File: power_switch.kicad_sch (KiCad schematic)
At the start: 0 parts

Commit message: split into multiple sheets
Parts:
- added J3: Power Input, TerminalBlock_RND:TerminalBlock_RND_205-00287_1x02_P5.08mm_Horizontal, symbol Connector:Screw_Terminal_01x02
- added J4: Power Output, TerminalBlock_RND:TerminalBlock_RND_205-00287_1x02_P5.08mm_Horizontal, symbol Connector:Screw_Terminal_01x02
- added R1, R2, R3: 4.7kΩ, symbol Device:R_Small
- added R4: 1.2kΩ, symbol Device:R_Small
- added U1: BTS7004-1EPP, Package_SO:Infineon_PG-TSDSO-14-22, symbol Power_Management:BTS7004-1EPP
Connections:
- new net: R1.2, U1.2 (IN)
- new net: R3.2, R4.2, U1.4 (IS)
- new net: J4.1 (Pin_1), U1.10 (OUT), U1.12 (OUT), U1.13 (OUT), U1.14 (OUT), U1.8 (OUT), U1.9 (OUT)
- new net: R2.2, U1.3 (DEN)
- new net GND: J3.2 (Pin_2), J4.2 (Pin_2), R4.1, U1.1 (GND)
- new net SW1_ADC: R3.1
- new net SW1_DEN: R2.1
- new net SW1_IN: R1.1
- new net VDD: J3.1 (Pin_1), U1.15 (VS)
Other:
- note added: "Power Input"
- note added: "Power Switch 1"

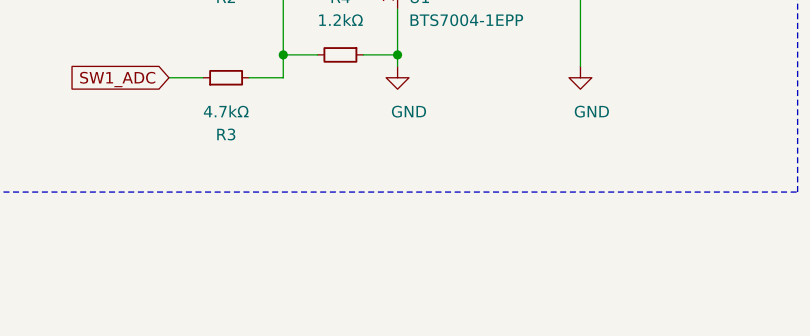
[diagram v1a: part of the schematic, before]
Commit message: use USB-C and add analog filtering
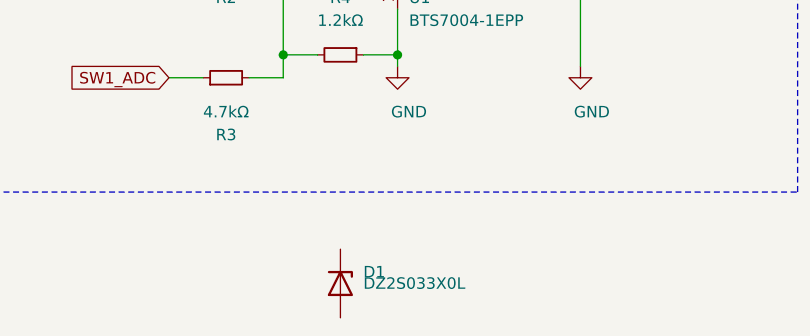
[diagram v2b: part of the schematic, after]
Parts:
- added D1: DZ2S033X0L, Diode_SMD:D_SOT-23_ANK, symbol Diode:DZ2S033X0L
- R1, R2, R3, R4: footprint (none) -> Resistor_SMD:R_0402_1005Metric
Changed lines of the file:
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@@
     (property "Reference" "R1" (id 0) (at 53.34 64.77 90))
     (property "Value" "4.7kΩ" (id 1) (at 53.34 67.31 90))
-    (property "Footprint" "" (id 2) (at 53.34 72.898 90)
+    (property "Footprint" "Resistor_SMD:R_0402_1005Metric" (id 2) (at 53.34 72.898 90)
       (effects (font (size 1.27 1.27)) hide)
     )
@@
     (property "Reference" "R2" (id 0) (at 53.34 80.01 90))
     (property "Value" "4.7kΩ" (id 1) (at 53.34 77.47 90))
-    (property "Footprint" "" (id 2) (at 53.34 75.438 90)
+    (property "Footprint" "Resistor_SMD:R_0402_1005Metric" (id 2) (at 53.34 75.438 90)
       (effects (font (size 1.27 1.27)) hide)
     )
@@
     (property "Reference" "R3" (id 0) (at 53.34 95.25 90))
     (property "Value" "4.7kΩ" (id 1) (at 53.34 92.71 90))
-    (property "Footprint" "" (id 2) (at 53.34 90.678 90)
+    (property "Footprint" "Resistor_SMD:R_0402_1005Metric" (id 2) (at 53.34 90.678 90)
       (effects (font (size 1.27 1.27)) hide)
     )
@@
     (property "Reference" "R4" (id 0) (at 66.04 80.01 90))
     (property "Value" "1.2kΩ" (id 1) (at 66.04 82.55 90))
-    (property "Footprint" "" (id 2) (at 66.04 84.582 90)
+    (property "Footprint" "Resistor_SMD:R_0402_1005Metric" (id 2) (at 66.04 84.582 90)
       (effects (font (size 1.27 1.27)) hide)
     )
@@
       (effects (font (size 1.27 1.27)) hide)
     )
+  )
+  (symbol (lib_id "Diode:DZ2S033X0L") (at 66.04 111.76 270) (unit 1)
+    (in_bom yes) (on_board yes)
+    (property "Reference" "D1" (id 0) (at 68.58 110.49 90)
+      (effects (font (size 1.27 1.27)) (justify left))
+    )
+    (property "Value" "DZ2S033X0L" (id 1) (at 68.58 111.76 90)
+      (effects (font (size 1.27 1.27)) (justify left))
+    )
+    (property "Footprint" "Diode_SMD:D_SOT-23_ANK" (id 2) (at 61.595 111.76 0)
+      (effects (font (size 1.27 1.27)) hide)
+    )
+    (property "Datasheet" "https://industrial.panasonic.com/content/data/SC/ds/ds4/DZ2S03300L_E.pdf" (id 3) (at 66.04 111.76 0)
+      (effects (font (size 1.27 1.27)) hide)
+    )

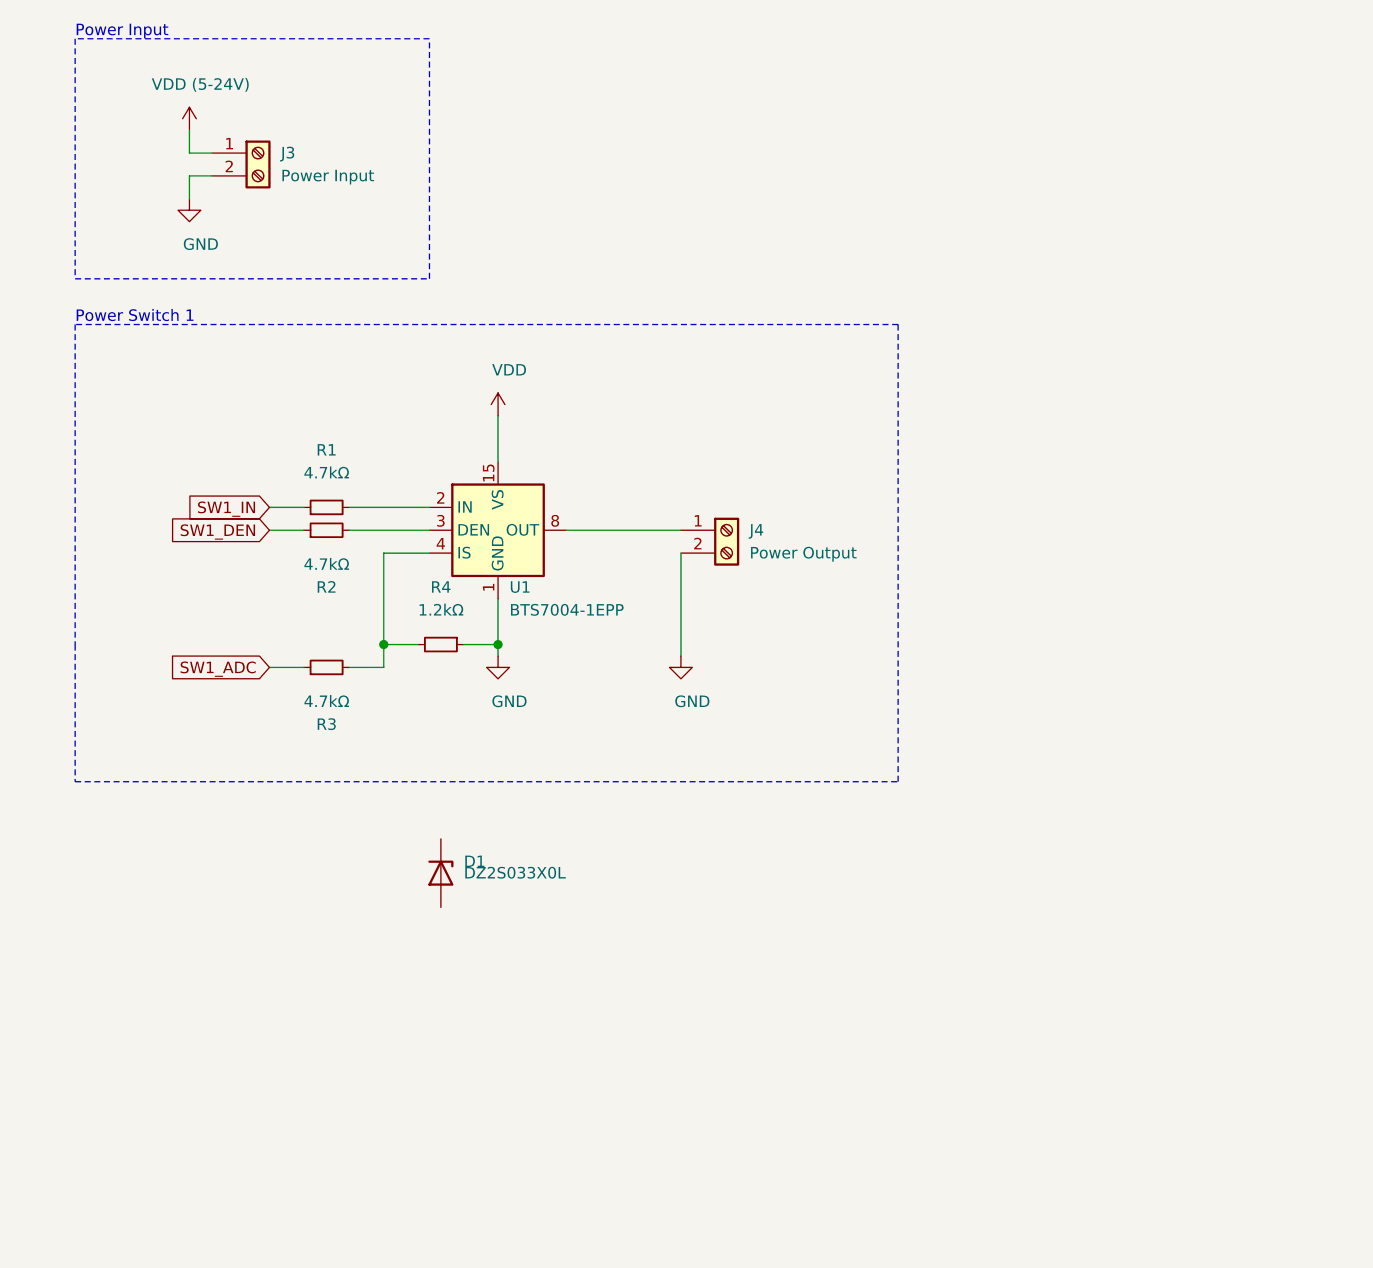
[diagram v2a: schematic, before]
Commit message: complete current sense circuit, add leds
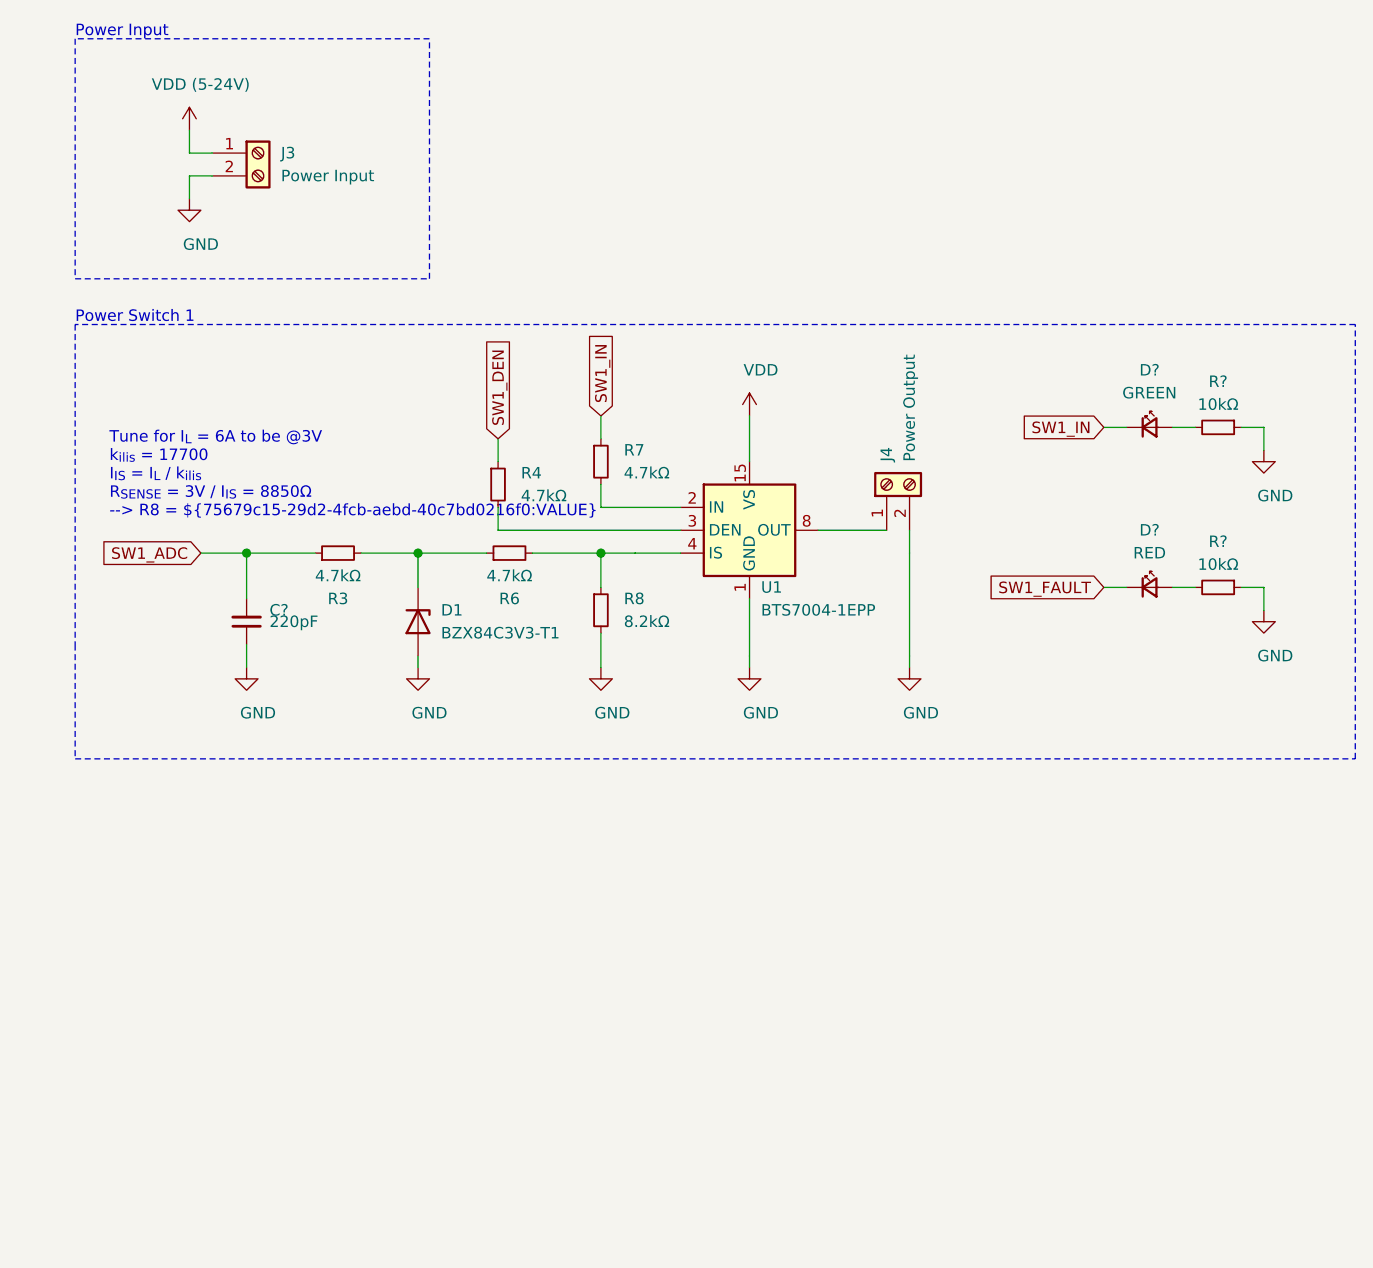
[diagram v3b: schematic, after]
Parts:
- removed R1, R2: 4.7kΩ, Resistor_SMD:R_0402_1005Metric, symbol Device:R_Small
- added C?: 220pF, symbol Device:C_Small
- added D?: RED, symbol Device:LED_Small
- added D?: GREEN, symbol Device:LED_Small
- added R6: 4.7kΩ, Resistor_SMD:R_0402_1005Metric, symbol Device:R_Small
- added R7: 4.7kΩ, symbol Device:R_Small
- added R8: 8.2kΩ, symbol Device:R_Small
- added R? (x2): 10kΩ, Resistor_SMD:R_0402_1005Metric, symbol Device:R_Small
- D1: value DZ2S033X0L -> BZX84C3V3-T1
- R4: value 1.2kΩ -> 4.7kΩ; footprint Resistor_SMD:R_0402_1005Metric -> (none)
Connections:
- net GND: now also D1.2 (A), C?.1, R8.2, R?.1, R?.1; no longer R4.1
- net SW1_ADC: now also C?.2
- net SW1_DEN: now also R4.1
- net SW1_IN: now also D?.1 (K), R7.1
- net at U1.2 (IN): now also R7.2
- net at D1.1 (K): now also R3.2, R6.1
- net at U1.3 (DEN): now also R4.2
- new net: D?.2 (A), R?.2 (x2)
- new net: R6.2, R8.1, U1.4 (IS)
- new net SW1_FAULT: D?.1 (K)
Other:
- note added: "Tune for I_{L} = 6A to be @3V k_{ilis} = 17700 I_{IS} = I_{L} / k_{ilis} R_{SENSE} = 3V / I_{IS} = 8850Ω --> R8 = ${75679c15-29d2-4fcb-aebd-40c7bd0216f0:VALUE}"
- moved on the sheet: D1, J4, R3, U1

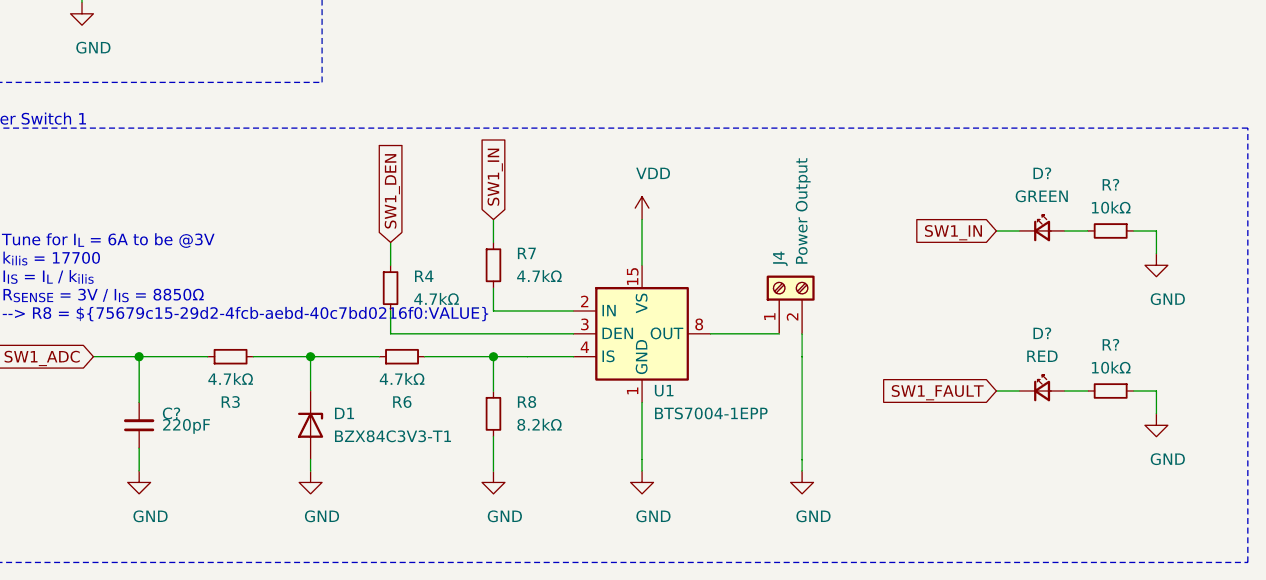
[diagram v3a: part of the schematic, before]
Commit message: fix LEDs, add power LED
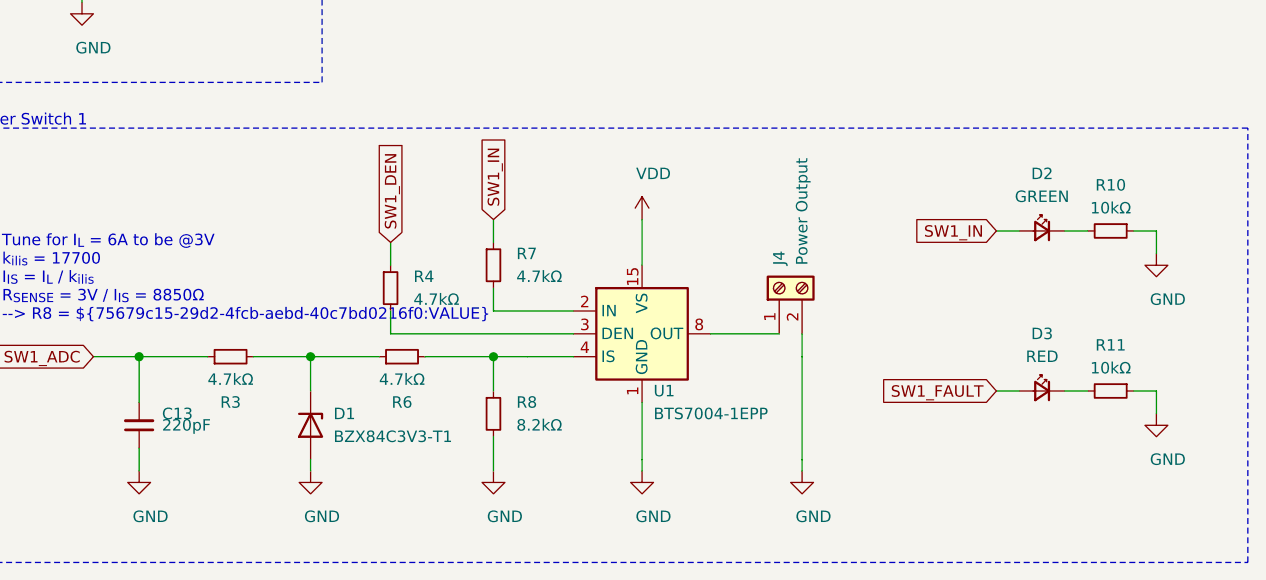
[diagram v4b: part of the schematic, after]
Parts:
- C13: renamed from C?; footprint (none) -> Capacitor_SMD:C_0402_1005Metric
- D2, D3: renamed from D?; footprint (none) -> LED_SMD:LED_0402_1005Metric
- R4, R7, R8: footprint (none) -> Resistor_SMD:R_0402_1005Metric
- gave numbers to parts that had none: 2
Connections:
- net SW1_FAULT: now also D3.2 (A); no longer D3.1 (K)
- net SW1_IN: now also D2.2 (A); no longer D2.1 (K)
- net at R11.2: now also D3.1 (K); no longer D3.2 (A)
- net at R10.2: now also D2.1 (K); no longer D2.2 (A)
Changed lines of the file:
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@@
   (symbol (lib_id "power:GND") (at 44.45 88.9 0) (unit 1)
     (in_bom yes) (on_board yes)
-    (property "Reference" "#PWR?" (id 0) (at 44.45 95.25 0)
+    (property "Reference" "#PWR0101" (id 0) (at 44.45 95.25 0)
       (effects (font (size 1.27 1.27)) hide)
     )
@@
   (symbol (lib_id "power:GND") (at 157.48 64.77 0) (unit 1)
     (in_bom yes) (on_board yes)
-    (property "Reference" "#PWR?" (id 0) (at 157.48 71.12 0)
+    (property "Reference" "#PWR0102" (id 0) (at 157.48 71.12 0)
       (effects (font (size 1.27 1.27)) hide)
     )
@@
   (symbol (lib_id "power:GND") (at 157.48 82.55 0) (unit 1)
     (in_bom yes) (on_board yes)
-    (property "Reference" "#PWR?" (id 0) (at 157.48 88.9 0)
+    (property "Reference" "#PWR0103" (id 0) (at 157.48 88.9 0)
       (effects (font (size 1.27 1.27)) hide)
     )
@@
       (effects (font (size 1.27 1.27)) (justify left))
     )
-    (property "Footprint" "" (id 2) (at 72.39 68.58 0)
+    (property "Footprint" "Resistor_SMD:R_0402_1005Metric" (id 2) (at 72.39 68.58 0)
       (effects (font (size 1.27 1.27)) hide)
     )
@@
       (effects (font (size 1.27 1.27)) (justify left))
     )
-    (property "Footprint" "" (id 2) (at 83.82 66.04 0)
+    (property "Footprint" "Resistor_SMD:R_0402_1005Metric" (id 2) (at 83.82 66.04 0)
       (effects (font (size 1.27 1.27)) hide)
     )
@@
       (effects (font (size 1.27 1.27)) (justify left))
     )
-    (property "Footprint" "" (id 2) (at 83.82 82.55 0)
+    (property "Footprint" "Resistor_SMD:R_0402_1005Metric" (id 2) (at 83.82 82.55 0)
       (effects (font (size 1.27 1.27)) hide)
     )
@@
   (symbol (lib_id "Device:R_Small") (at 152.4 62.23 270) (unit 1)
     (in_bom yes) (on_board yes)
-    (property "Reference" "R?" (id 0) (at 152.4 57.15 90))
+    (property "Reference" "R10" (id 0) (at 152.4 57.15 90))
     (property "Value" "10kΩ" (id 1) (at 152.4 59.69 90))
     (property "Footprint" "Resistor_SMD:R_0402_1005Metric" (id 2) (at 152.4 60.452 90)
@@
   (symbol (lib_id "Device:R_Small") (at 152.4 80.01 270) (unit 1)
     (in_bom yes) (on_board yes)
-    (property "Reference" "R?" (id 0) (at 152.4 74.93 90))
+    (property "Reference" "R11" (id 0) (at 152.4 74.93 90))
     (property "Value" "10kΩ" (id 1) (at 152.4 77.47 90))
     (property "Footprint" "Resistor_SMD:R_0402_1005Metric" (id 2) (at 152.4 78.232 90)
@@
     )
   )
-  (symbol (lib_id "Device:LED_Small") (at 144.78 62.23 0) (unit 1)
-    (in_bom yes) (on_board yes)
-    (property "Reference" "D?" (id 0) (at 144.78 55.88 0))
+  (symbol (lib_id "Device:LED_Small") (at 144.78 62.23 0) (mirror y) (unit 1)
+    (in_bom yes) (on_board yes)
+    (property "Reference" "D2" (id 0) (at 144.78 55.88 0))
     (property "Value" "GREEN" (id 1) (at 144.78 58.42 0))
-    (property "Footprint" "" (id 2) (at 144.78 62.23 90)
+    (property "Footprint" "LED_SMD:LED_0402_1005Metric" (id 2) (at 144.78 62.23 90)
       (effects (font (size 1.27 1.27)) hide)
     )
@@
     )
   )
-  (symbol (lib_id "Device:LED_Small") (at 144.78 80.01 0) (unit 1)
-    (in_bom yes) (on_board yes)
-    (property "Reference" "D?" (id 0) (at 144.78 73.66 0))
+  (symbol (lib_id "Device:LED_Small") (at 144.78 80.01 0) (mirror y) (unit 1)
+    (in_bom yes) (on_board yes)
+    (property "Reference" "D3" (id 0) (at 144.78 73.66 0))
     (property "Value" "RED" (id 1) (at 144.78 76.2 0))
-    (property "Footprint" "" (id 2) (at 144.78 80.01 90)
+    (property "Footprint" "LED_SMD:LED_0402_1005Metric" (id 2) (at 144.78 80.01 90)
       (effects (font (size 1.27 1.27)) hide)
     )
@@
   (symbol (lib_id "Device:C_Small") (at 44.45 83.82 180) (unit 1)
     (in_bom yes) (on_board yes)
-    (property "Reference" "C?" (id 0) (at 46.99 82.55 0)
+    (property "Reference" "C13" (id 0) (at 46.99 82.55 0)
       (effects (font (size 1.27 1.27)) (justify right))
     )
@@
       (effects (font (size 1.27 1.27)) (justify right))
     )
-    (property "Footprint" "" (id 2) (at 44.45 83.82 0)
-      (effects (font (size 1.27 1.27)) hide)
-    )
+    (property "Footprint" "Capacitor_SMD:C_0402_1005Metric" (id 2) (at 44.45 83.82 0)
+      (effects (font (size 1.27 1.27)) hide)
+    )
